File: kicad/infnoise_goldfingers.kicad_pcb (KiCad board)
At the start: 2 copper layers, 34.8 x 12.2 mm, 28 parts, among them SW1 MC74VHC1G66DFT1G, SW2 MC74VHC1G66DFT1G, X1 USBRAWPINS

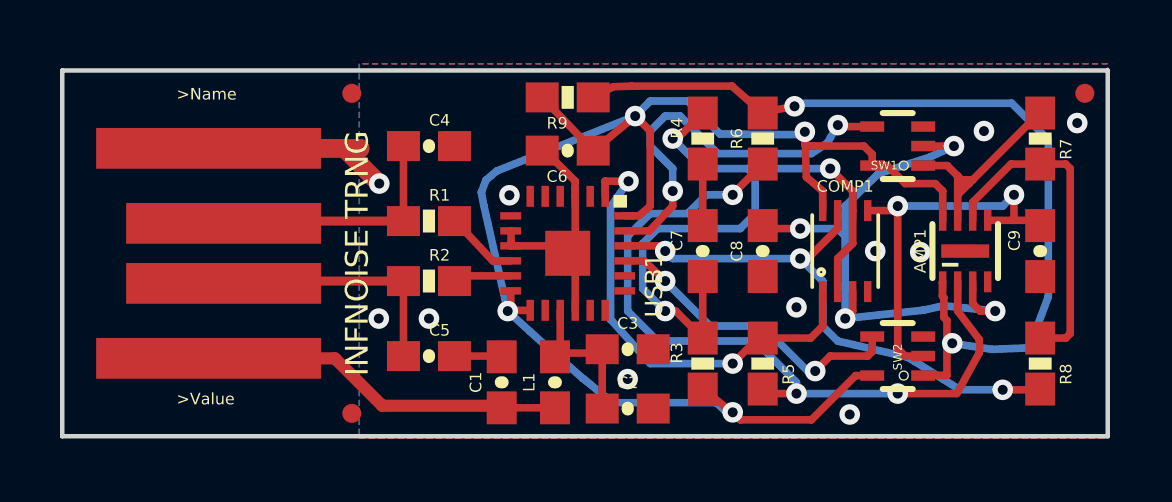
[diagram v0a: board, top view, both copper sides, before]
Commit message: bring into KiCad 9; fix errors in last import
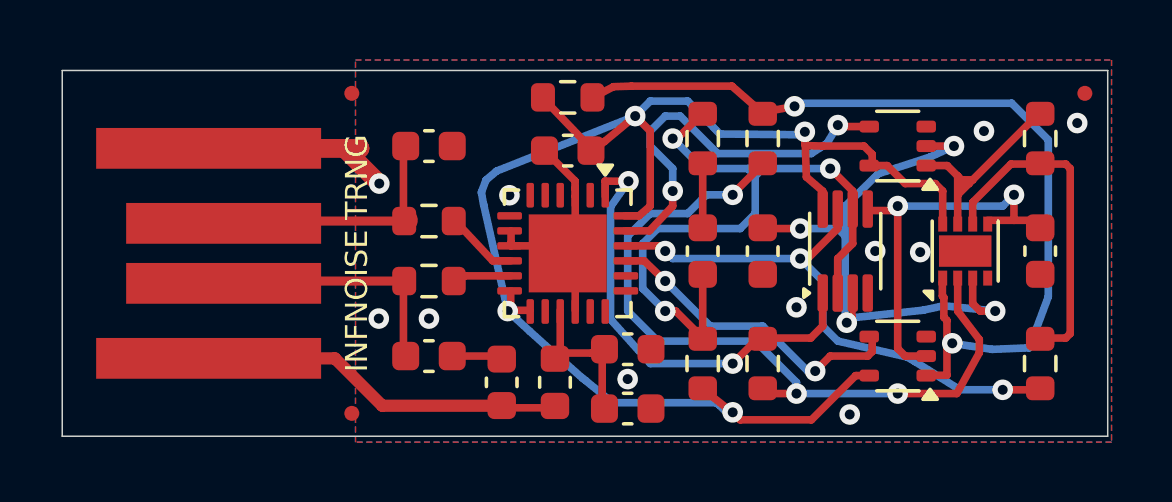
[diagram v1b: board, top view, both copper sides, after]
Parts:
- AMP1: footprint DFN8-2X3 -> Package_DFN_QFN:DFN-8-1EP_2x2mm_P0.5mm_EP1.05x1.75mm
- C1, C7: value 10nF -> 0.01 µF; footprint 0603-CAP -> Capacitor_SMD:C_0603_1608Metric
- C2: value 4.7uF -> 4.7 µF; footprint 0603-CAP -> Capacitor_SMD:C_0603_1608Metric
- C3, C6: value 100nF -> 0.1 µF; footprint 0603-CAP -> Capacitor_SMD:C_0603_1608Metric
- C4, C5: value 47pF -> 47 pF; footprint 0603-CAP -> Capacitor_SMD:C_0603_1608Metric
- C8, C9: value 220pF -> 220 pF; footprint 0603-CAP -> Capacitor_SMD:C_0603_1608Metric
- COMP1: value TC75W57FK -> TC75W57FKTE85LF; footprint SSOP8-P-0.50A -> Package_SO:VSSOP-8_2.3x2mm_P0.5mm
- FID1, FID2, FID3: footprint MICRO-FIDUCIAL -> Fiducial:Fiducial_0.5mm_Mask1mm
- L1: value FERRITE-BEAD0603-IND -> BLM18AG601SN1D; footprint 0603-IND -> Inductor_SMD:L_0603_1608Metric
- R1, R2: value 27 -> 27 Ω; footprint 0603-RES -> Resistor_SMD:R_0603_1608Metric
- R3, R4, R5, R8, R9: value 10K -> 10 kΩ; footprint 0603-RES -> Resistor_SMD:R_0603_1608Metric
- R6, R7: value 8.2K -> 8.2 kΩ; footprint 0603-RES -> Resistor_SMD:R_0603_1608Metric
- SW1, SW2: value MC74VHC1G66DFT1G -> NS5B1G385DFT2G; footprint SC70-5L -> Package_TO_SOT_SMD:SOT-353_SC-70-5
- USB1: footprint QFN24-4X4 -> Package_DFN_QFN:QFN-24-1EP_4x4mm_P0.5mm_EP2.6x2.6mm
- X1: value USBRAWPINS -> USB_A; footprint USB-A-RAWPINS -> infnoise_goldfingers:USB-A-RAWPINS
- turned AMP1 to 90 degrees
- turned COMP1 to 90 degrees
- turned SW1 to 180 degrees
- turned SW2 to 180 degrees
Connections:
- net /VCC renamed +5V
- net /VCC33 renamed +3.3V
- C1 pad 1: /VCCIN -> Net-(X1-VBUS)
- C4 pad 1: /USB_P -> Net-(X1-D+)
- C5 pad 1: /USB_M -> Net-(X1-D-)
- L1 pad 1: /VCCIN -> Net-(X1-VBUS)
- R1 pad 1: /USB_P -> Net-(X1-D+)
- R2 pad 1: /USB_M -> Net-(X1-D-)
- USB1 pad 14: Net-(USB1-Pad14) -> unconnected-(USB1-VCORE-Pad14)
- USB1 pad 17: Net-(USB1-Pad17) -> unconnected-(USB1-~{TXE}-Pad17)
- USB1 pad 18: Net-(USB1-Pad18) -> unconnected-(USB1-~{RXF}-Pad18)
- USB1 pad 19: Net-(USB1-Pad19) -> unconnected-(USB1-CBUS6-Pad19)
- USB1 pad 2: Net-(USB1-Pad2) -> unconnected-(USB1-DATA7-Pad2)
- USB1 pad 20: Net-(USB1-Pad20) -> unconnected-(USB1-CBUS5-Pad20)
- USB1 pad 4: Net-(USB1-Pad4) -> unconnected-(USB1-DATA5-Pad4)
- USB1 pad 5: Net-(USB1-Pad5) -> unconnected-(USB1-DATA6-Pad5)
- USB1 pad 6: Net-(USB1-Pad6) -> unconnected-(USB1-DATA3-Pad6)
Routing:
- net /USB_P: track 14.7 -> 0.00 mm
- net Net-(X1-VBUS): track 0.00 -> 12.2 mm
- net /VCCIN: track 12.2 -> 0.00 mm
- net Net-(X1-D+): track 0.00 -> 8.67 mm
- net Net-(X1-D-): track 0.00 -> 8.57 mm
- net /USB_M: track 2.50 -> 0.00 mm
- net GND: vias 1 -> 11
- net (no net): vias 10 -> 0
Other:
- net class Default removed
- rule pad_to_mask_clearance: 0.2 -> 0
